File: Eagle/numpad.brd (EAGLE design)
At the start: 78 x 105 mm, 19 parts, among them SW1 SWITCH-SMD-SCHURTER-1241.1612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, U1 PROMICRO

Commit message: moved files due to eagle error
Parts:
- removed U$10, U$11, U$12, U$13, U$14, U$4, U$5, U$6, U$7, U$8, U$9: KEYSWITCH-PLATE-MXPLATE-1U, Keyboard:MXPLATE-1U
- removed U$15: KEYSWITCH-PLATE-MXPLATE-2U, Keyboard:MXPLATE-2U
- removed U$16, U$17: KEYSWITCH-PLATE-MXPLATE-2U-ROTATED, Keyboard:MXPLATE-2U-ROTATED
- added D1, D10, D11, D12, D13, D14, D15, D16, D17, D2, D3, D4, D5, D6, D7, D8, D9: (no value), Components:DIODE_HAND
- added U$19, U$20, U$21, U$22, U$23, U$24, U$25, U$26, U$27, U$28, U$29, U$30, U$31, U$32: KEYSWITCH-PLAIN-MX-1U, Keyboard:MX-1U
- U$1: value KEYSWITCH-PLATE-MXPLATE-1U -> KEYSWITCH-PLAIN-MX-2U; device Keyboard:MXPLATE-1U -> Keyboard:MX-2U
- U$2, U$3: value KEYSWITCH-PLATE-MXPLATE-1U -> KEYSWITCH-PLAIN-MX-2U-ROTATED; device Keyboard:MXPLATE-1U -> Keyboard:MX-2U-ROTATED
- moved U$1 372.6 mm to (15.0, -335.0)
- moved U$2 369.0 mm to (-9.00, -331.0)
- moved U$3 358.9 mm to (-28.0, -331.0)

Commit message: finished first test of board, need to finish placement of switches
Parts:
- removed U$19, U$22, U$32: KEYSWITCH-PLAIN-MX-1U, Keyboard:MX-1U
- added BOTTOM1, TOPLEFT, TOPRIGHT: KEYSWITCH-PLAIN-MX-1U, Keyboard:MX-1U
- U$1: value KEYSWITCH-PLAIN-MX-2U -> KEYSWITCH-PLAIN-MX-2U-FLIPPED; device Keyboard:MX-2U -> Keyboard:MX-2U-FLIPPED
- moved U$2 407.3 mm to (85.7, 65.2)
- moved U$3 375.7 mm to (86.0, 27.0)
- moved U$1 353.4 mm to (38.1, 17.6)
- moved U$31 346.1 mm to (67.0, 37.0)
- moved U$30 328.4 mm to (48.0, 37.0)
- moved U$28 315.7 mm to (29.0, 56.0)
- moved U$29 311.3 mm to (28.8, 36.6)
- moved U$27 302.7 mm to (48.0, 56.0)
- moved U$25 295.0 mm to (67.0, 75.0)
- moved U$26 291.0 mm to (67.0, 56.0)
- moved U$24 276.9 mm to (48.0, 75.0)
- moved U$23 259.8 mm to (29.0, 75.0)
- moved U$21 254.9 mm to (67.0, 94.0)
- moved U$20 236.4 mm to (48.0, 94.0)
- moved D4 132.2 mm to (85.0, 84.0)
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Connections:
- new net N$10: D6.A1, D6.A2, D6.A3, U$24.MX1
- new net N$11: D7.A1, D7.A2, D7.A3, U$25.MX1
- new net N$12: D8.A1, D8.A2, D8.A3, U$2.MX1
- new net N$13: D9.A1, D9.A2, D9.A3, U$26.MX1
- new net N$14: D10.A1, D10.A2, D10.A3, U$27.MX1
- new net N$15: D11.A1, D11.A2, D11.A3, U$28.MX1
- new net N$16: D12.A1, D12.A2, D12.A3, U$29.MX1
- new net N$17: D13.A1, D13.A2, D13.A3, U$30.MX1
- new net N$18: D14.A1, D14.A2, D14.A3, U$31.MX1
- new net N$19: BOTTOM1.MX1, D16.A1, D16.A2, D16.A3
- new net N$2: D1.A1, D1.A2, D1.A3, TOPLEFT.MX1
- new net N$20: D17.A1, D17.A2, D17.A3, U$1.MX1
- new net N$21: D15.A1, D15.A2, D15.A3, U$3.MX1
- new net N$22: D15.C1, D15.C2, D15.C3, D16.C1, D16.C2, D16.C3, D17.C1, D17.C2, D17.C3, U1.5
- new net N$23: D12.C1, D12.C2, D12.C3, D13.C1, D13.C2, D13.C3, D14.C1, D14.C2, D14.C3, U1.6
- new net N$24: D10.C1, D10.C2, D10.C3, D11.C1, D11.C2, D11.C3, D9.C1, D9.C2, D9.C3, U1.7
- new net N$26: D5.C1, D5.C2, D5.C3, D6.C1, D6.C2, D6.C3, D7.C1, D7.C2, D7.C3, D8.C1, D8.C2, D8.C3, U1.8
- new net N$27: BOTTOM1.MX2, U$21.MX2, U$25.MX2, U$26.MX2, U$31.MX2, U1.14
- new net N$3: D2.A1, D2.A2, D2.A3, U$20.MX1
- new net N$30: TOPRIGHT.MX2, U$2.MX2, U$3.MX2, U1.15
- new net N$4: D3.A1, D3.A2, D3.A3, U$21.MX1
- new net N$5: D4.A1, D4.A2, D4.A3, TOPRIGHT.MX1
- new net N$6: D1.C1, D1.C2, D1.C3, D2.C1, D2.C2, D2.C3, D3.C1, D3.C2, D3.C3, D4.C1, D4.C2, D4.C3, U1.9
- new net N$7: TOPLEFT.MX2, U$1.MX2, U$23.MX2, U$28.MX2, U$29.MX2, U1.10
- new net N$8: D5.A1, D5.A2, D5.A3, U$23.MX1
- new net N$9: U$20.MX2, U$24.MX2, U$27.MX2, U$30.MX2, U1.16
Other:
- board size 78 x 105 mm -> 95 x 99 mm

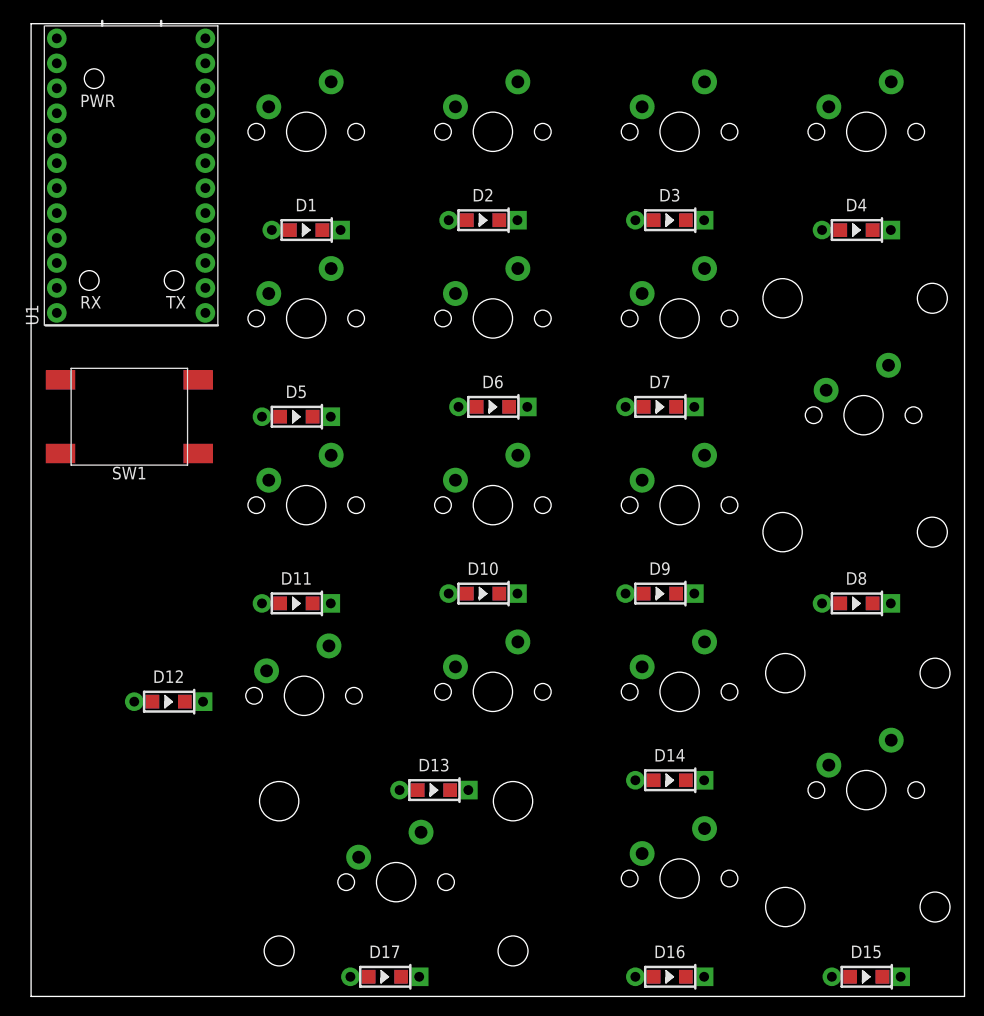
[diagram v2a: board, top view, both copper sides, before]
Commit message: deleted old testing folder
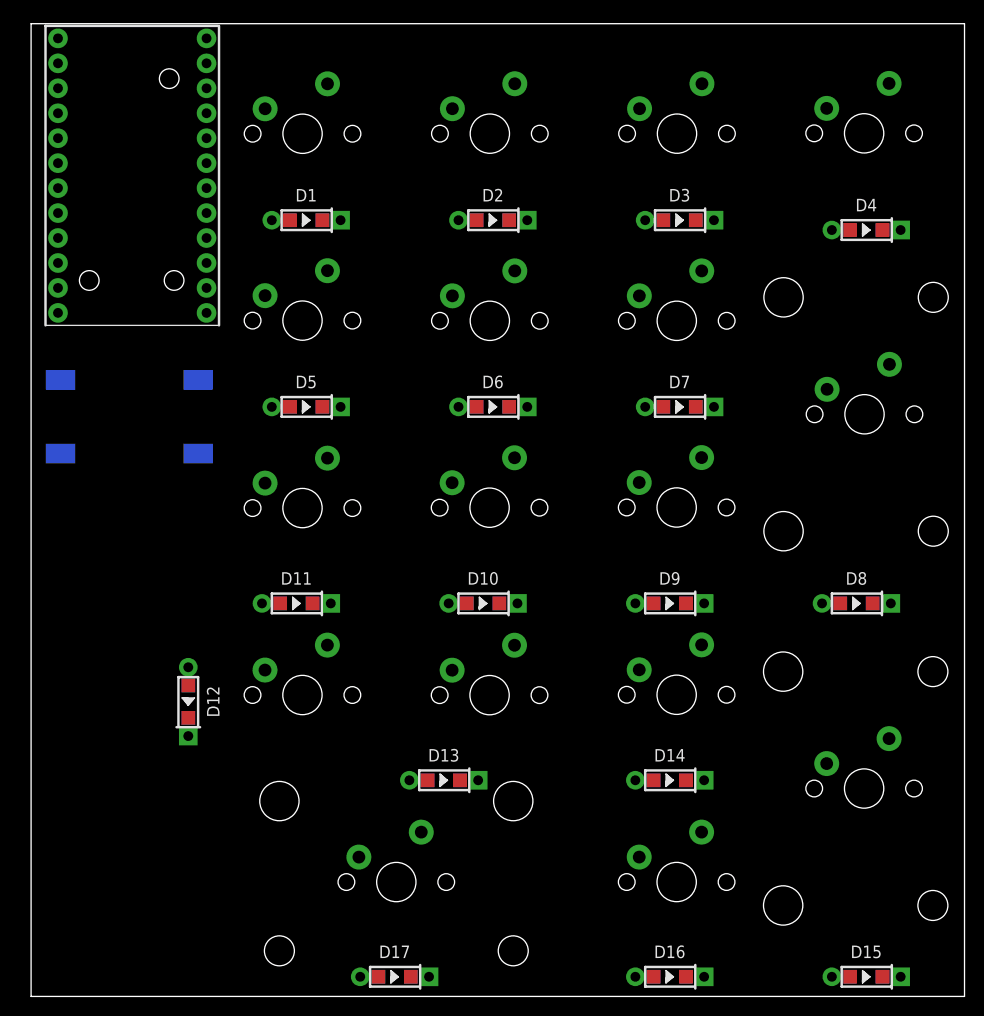
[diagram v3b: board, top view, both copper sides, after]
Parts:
- moved D12 2.00 mm to (17.0, 36.0), turned to 270 degrees
- moved D7 2.00 mm to (67.0, 66.0)
- moved D13 1.41 mm to (43.0, 28.0)
- moved D5 1.41 mm to (29.0, 66.0)
- moved D9 1.41 mm to (66.0, 46.0)
- moved D1 1.00 mm to (29.0, 85.0)
- moved D10 1.00 mm to (47.0, 46.0)
- moved D17 1.00 mm to (38.0, 8.00)
- moved D2 1.00 mm to (48.0, 85.0)
- moved D3 1.00 mm to (67.0, 85.0)
- moved D4 1.00 mm to (86.0, 84.0)
- moved U$28 0.48 mm to (28.6, 55.7)
- moved U$30 0.48 mm to (47.7, 36.7)
- moved BOTTOM1 0.46 mm to (66.7, 17.6)
- moved U$23 0.44 mm to (28.6, 74.8)
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
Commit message: added hole
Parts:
- D1, D10, D11, D12, D13, D14, D15, D16, D17, D2, D3, D4, D5, D6, D7, D8, D9: value (none) -> 1N4148; device Components:DIODE_HAND -> Components:DO-35
- moved D12 73.2 mm to (85.0, 9.00), turned to 180 degrees
- moved D15 72.8 mm to (18.0, 34.0), turned to 270 degrees
- moved D11 56.0 mm to (84.0, 46.0)
- moved D8 56.0 mm to (29.0, 46.0)
- moved D14 25.0 mm to (41.0, 27.0)
- moved D13 24.0 mm to (67.0, 27.0)
- moved D10 19.0 mm to (66.0, 46.0)
- moved D9 19.0 mm to (47.0, 46.0)
- moved SW1 6.64 mm to (14.2, 59.2), turned to 270 degrees
- moved U1 4.08 mm to (11.9, 85.5), flipped to the top
- moved D16 1.41 mm to (67.0, 9.00), turned to 180 degrees
- moved D4 1.41 mm to (87.0, 85.0)
- moved D5 1.41 mm to (28.0, 65.0)
- moved D7 1.41 mm to (66.0, 65.0)
- moved D1 1.00 mm to (29.0, 84.0)
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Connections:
- net N$27 renamed COL2
- net N$30 renamed COL3
- net N$7 renamed COL0
- net N$9 renamed COL1
- removed net N$16: D12.A1, D12.A2, D12.A3, U$29.MX1
- removed net N$22: D15.C1, D15.C2, D15.C3, D16.C1, D16.C2, D16.C3, D17.C1, D17.C2, D17.C3, U1.5
- removed net N$23: D12.C1, D12.C2, D12.C3, D13.C1, D13.C2, D13.C3, D14.C1, D14.C2, D14.C3, U1.6
- removed net N$24: D10.C1, D10.C2, D10.C3, D11.C1, D11.C2, D11.C3, D9.C1, D9.C2, D9.C3, U1.7
- removed net N$26: D5.C1, D5.C2, D5.C3, D6.C1, D6.C2, D6.C3, D7.C1, D7.C2, D7.C3, D8.C1, D8.C2, D8.C3, U1.8
- new net ROW0: D1.C, D2.C, D3.C, D4.C, U1.9
- new net ROW1: D5.C, D6.C, D7.C, U1.8
- new net ROW2: D10.C, D11.C, D8.C, D9.C, U1.7
- new net ROW3: D13.C, D14.C, D15.C, U1.6
- new net ROW4: D12.C, D16.C, D17.C, U1.5
- net N$10: now also D6.A; no longer D6.A1, D6.A2, D6.A3
- net N$11: now also D7.A; no longer D7.A1, D7.A2, D7.A3
- net N$12: now also D11.A; no longer D8.A1, D8.A2, D8.A3
- net N$13: now also D10.A; no longer D9.A1, D9.A2, D9.A3
- net N$14: now also D9.A; no longer D10.A1, D10.A2, D10.A3
- net N$15: now also D8.A; no longer D11.A1, D11.A2, D11.A3
- net N$17: now also D14.A; no longer D13.A1, D13.A2, D13.A3
- net N$18: now also D13.A; no longer D14.A1, D14.A2, D14.A3
- net N$19: now also D16.A; no longer D16.A1, D16.A2, D16.A3
- net N$2: now also D1.A; no longer D1.A1, D1.A2, D1.A3
- net N$20: now also D17.A; no longer D17.A1, D17.A2, D17.A3
- net N$21: now also D12.A; no longer D15.A1, D15.A2, D15.A3
- net N$3: now also D2.A; no longer D2.A1, D2.A2, D2.A3
- net N$4: now also D3.A; no longer D3.A1, D3.A2, D3.A3
- net N$5: now also D4.A; no longer D4.A1, D4.A2, D4.A3
- net N$6: now also D15.A, U$29.MX1; no longer D1.C1, D1.C2, D1.C3, D2.C1, D2.C2, D2.C3, D3.C1, D3.C2, D3.C3, D4.C1, D4.C2, D4.C3, U1.9
- net N$8: now also D5.A; no longer D5.A1, D5.A2, D5.A3
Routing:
- net COL3: track 0.00 -> 144.4 mm
- net COL2: track 0.00 -> 142.1 mm
- net ROW4: track 0.00 -> 135.2 mm
- net ROW3: track 0.00 -> 114.3 mm
- net ROW2: track 0.00 -> 109.3 mm
- net COL1: track 0.00 -> 105.8 mm
- net COL0: track 0.00 -> 101.0 mm
- net ROW0: track 0.00 -> 95.4 mm, vias 0 -> 1
- net ROW1: track 0.00 -> 73.4 mm
- net GND: track 0.00 -> 61.4 mm
- net N$1: track 0.00 -> 46.1 mm
- net N$21: track 0.00 -> 27.8 mm
- net N$12: track 0.00 -> 25.4 mm
- net N$20: track 0.00 -> 20.7 mm
- net N$19: track 0.00 -> 18.7 mm
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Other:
- board size 95 x 99 mm -> 94 x 95 mm

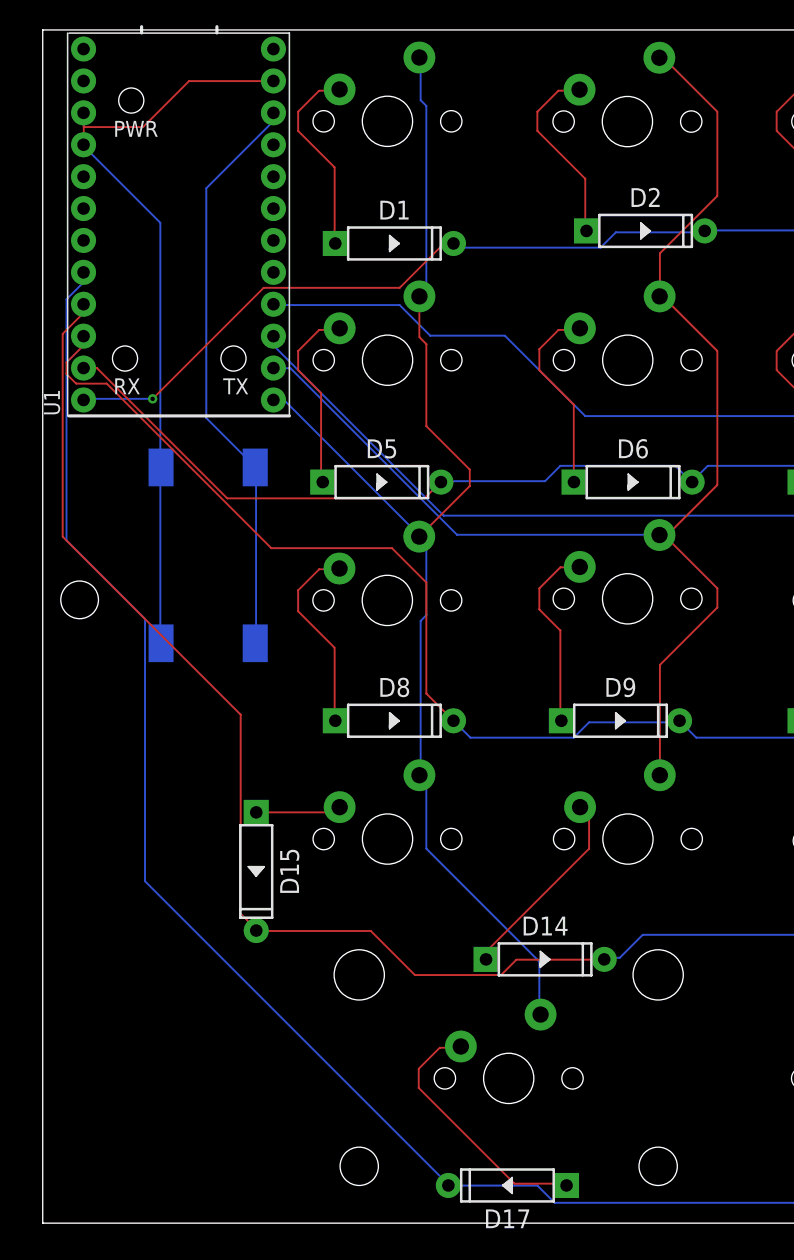
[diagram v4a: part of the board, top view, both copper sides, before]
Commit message: replaced promicro and relayed wire
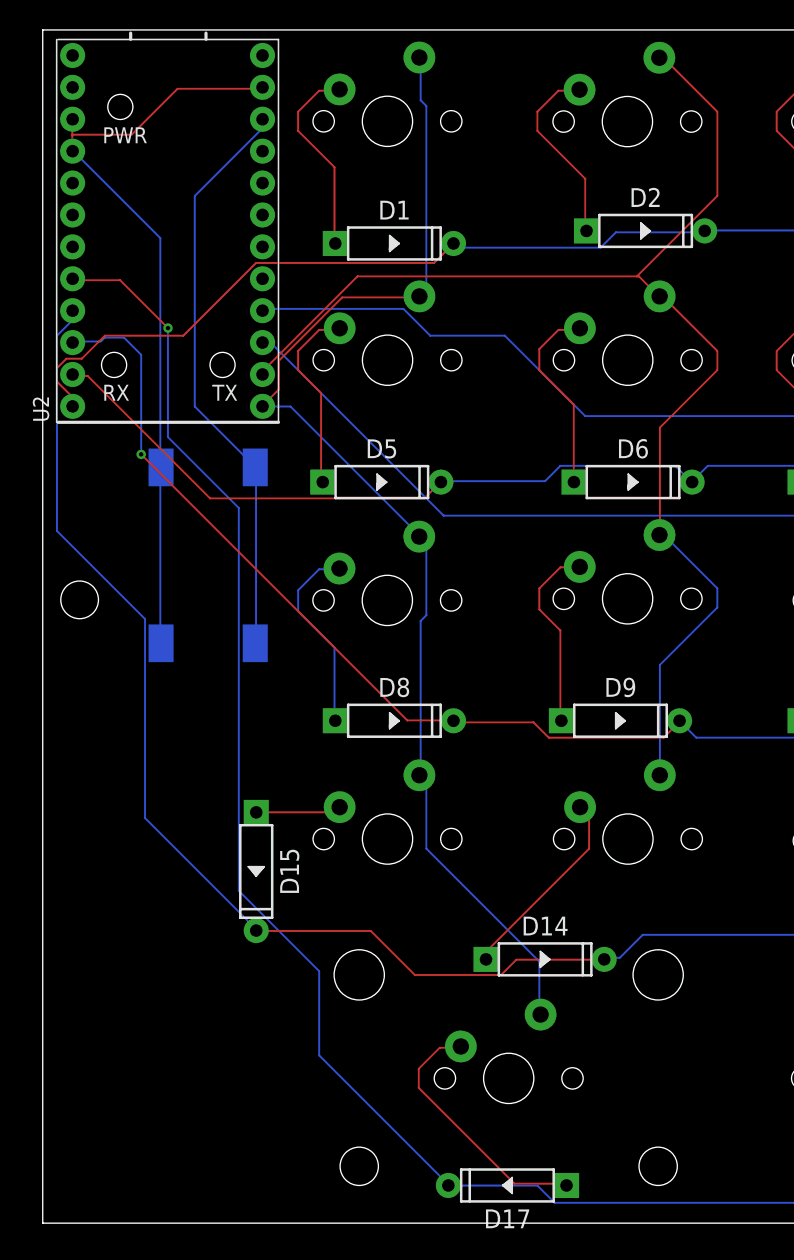
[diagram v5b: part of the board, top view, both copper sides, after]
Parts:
- removed U1: PROMICRO, MCU:PROMICRO
- added U2: PROMICRO, MCU:PROMICRO
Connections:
- net COL0: now also U2.10; no longer U1.10
- net COL1: now also U2.16; no longer U1.16
- net COL2: now also U2.14; no longer U1.14
- net COL3: now also U2.15; no longer U1.15
- net GND: now also U2.GND@23, U2.GND@3, U2.GND@4; no longer U1.GND@23, U1.GND@3, U1.GND@4
- net N$1: now also U2.RST; no longer U1.RST
- net ROW0: now also U2.9; no longer U1.9
- net ROW1: now also U2.8; no longer U1.8
- net ROW2: now also U2.7; no longer U1.7
- net ROW3: now also U2.6; no longer U1.6
- net ROW4: now also U2.5; no longer U1.5
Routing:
- net ROW0: track 95.4 -> 100.0 mm, vias 1 -> 0
- net COL0: track 101.0 -> 96.4 mm
- net ROW2: track 109.3 -> 106.1 mm, vias 0 -> 1
- net COL1: track 105.8 -> 104.0 mm
- net ROW4: track 135.2 -> 136.0 mm, vias 0 -> 1
- net COL3: track 144.4 -> 145.2 mm
- net ROW1: track 73.4 -> 74.1 mm
- net ROW3: track 114.3 -> 113.8 mm
